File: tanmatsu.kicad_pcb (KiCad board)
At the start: 4 copper layers, 114.9 x 129.9 mm, 362 parts, among them CN1 DF37NB-24DS-0.4V(51), J1 USB host, J10 External Add-On (SAO / PMOD), J11 Battery, J12 GND, J13 Sensor, J14 3.3v, J15 SDA, J16 SCL, J2 Micro_SD_Card, J3 USB device, J4 Headphone, J5 Speaker, J6 CAMERA, J7 SAO, J8 Expansion I3C, J9 Internal Add-On, Q1 AP2302B, Q2 AP2302B, Q3 AP2302B, Q4 AP2302B, SW1 Boot, SW2 User, SW3 Power, U1 USBLC6-2P6, U10 W25Q128JVS, U11 CH32V203C8T6, U12 74LVC2G02HD4-7, U13 Keyboard, U14 LR8341A-M25, U15 BQ25895RTW, U16 TPS63020DSJR, U17 AP3032KTR, U18 AP3032KTR, U19 SY6280AAC, U2 TPD4E05U06DQAR, U20 ESP32-C6-WROOM-1, U21 E22-900M22S, U22 74LVC1GU04, U23 IR968-8P(X1-X4)XBY, U24 ES8156, U25 FM8002A, U26 74LVC1G17GW,125, U27 SK6805, U28 SK6805, U29 SK6805, U3 CH334R, U30 SK6805, U31 SK6805, U32 SK6805, U33 BMI270, U4 USBLC6-2P6, U5 ESD, U6 ESD, U7 TLV62569DBV, U8 ESP32-P4, U9 TXB0104RGY, Y1 12MHz, Y2 40MHz, Y3 32.768KHz

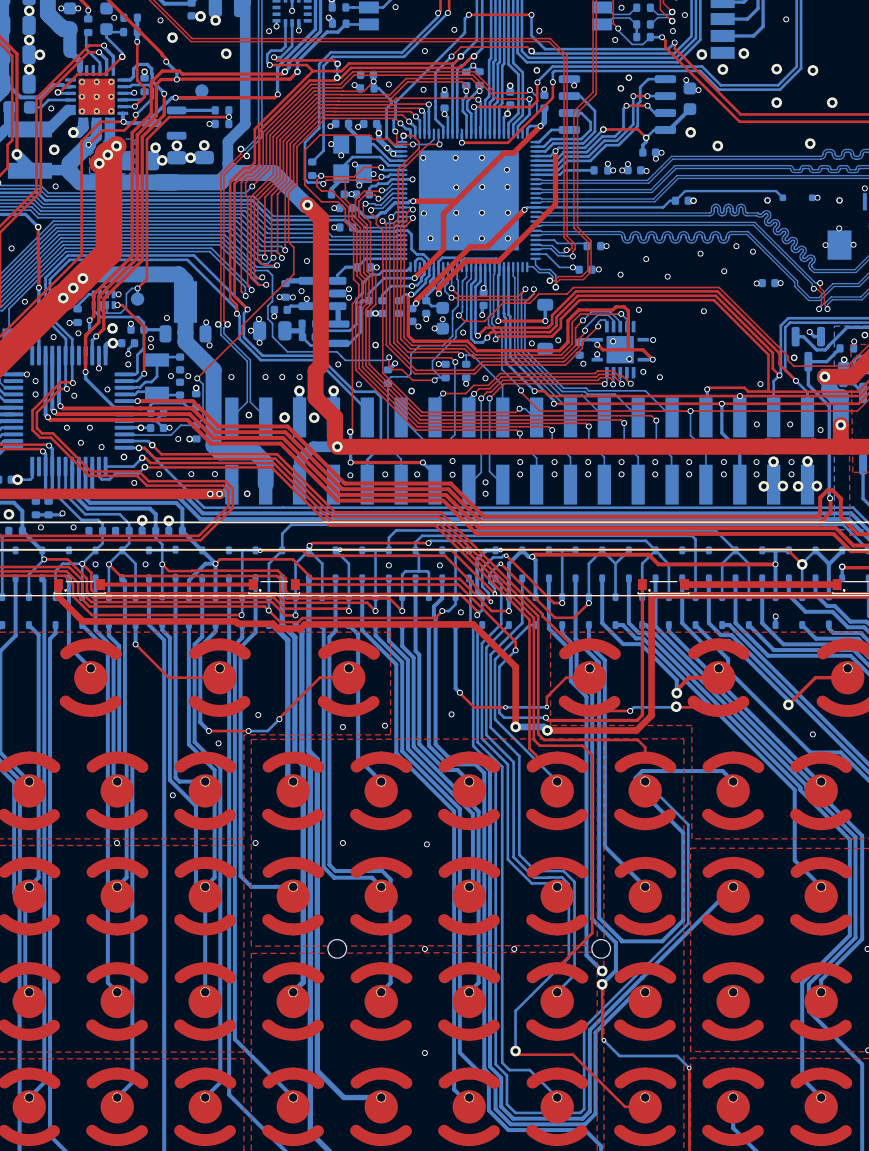
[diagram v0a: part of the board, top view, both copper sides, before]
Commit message: Replace remaining 0.2mm vias with 0.3mm vias (#15)
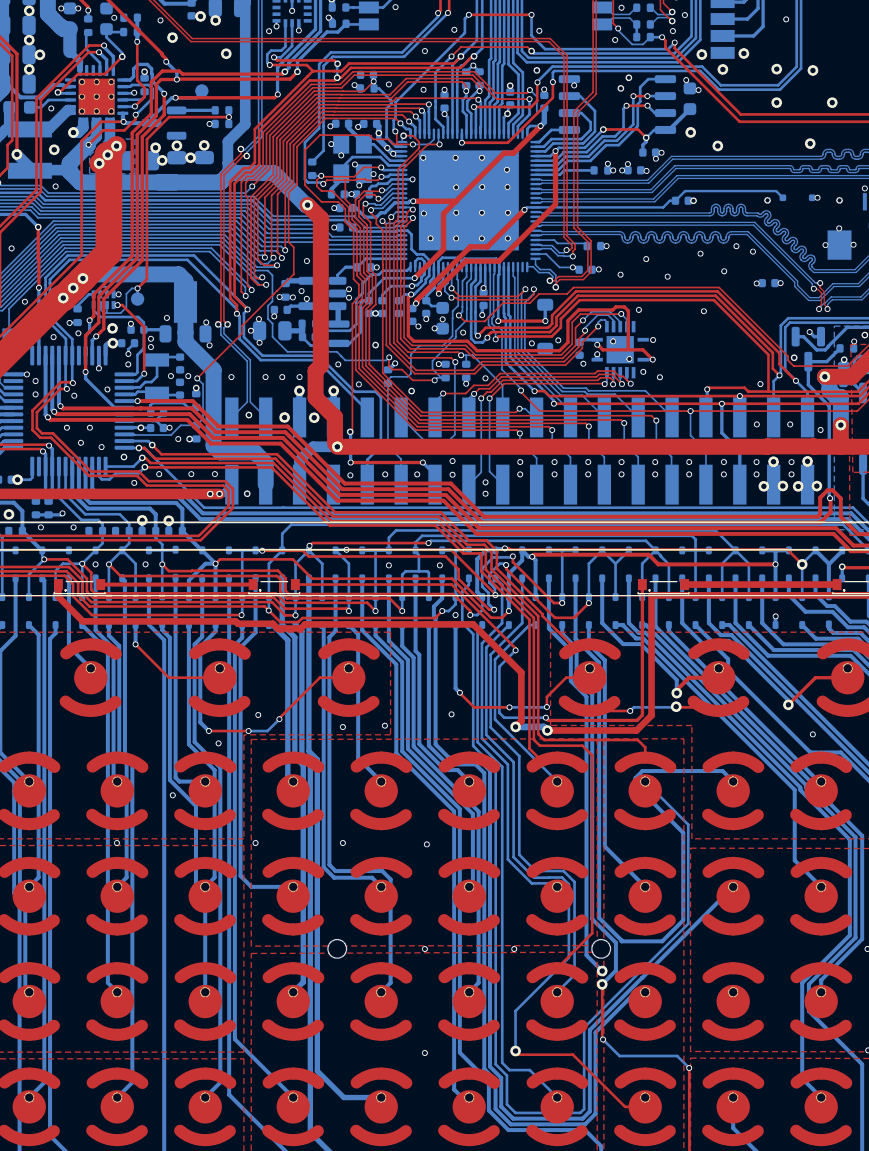
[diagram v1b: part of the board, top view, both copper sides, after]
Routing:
- net KB_COL4: track 84.9 -> 87.0 mm
- net KB_ROW5: track 49.4 -> 50.2 mm
- net KB_ROW8: track 117.7 -> 118.5 mm
- net KB_ROW4: track 68.4 -> 69.2 mm
- net KB_ROW3: track 48.9 -> 49.6 mm
